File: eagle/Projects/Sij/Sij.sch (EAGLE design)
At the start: 59 parts, among them U1 ATMEGA2560AU, U2 BQ76925_PW_20, U3 LM1085_KTT_3, U4 LM7805

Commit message: joué avec le schematic et la commande digikey
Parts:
- removed C1, C2: 20pF, SparkFun-Capacitors:22PF-50V-5%(0603)
- removed JUMP_3_CELL, JUMP_4_CELL, JUMP_5_CELL, JUMP_PWR_BAT, JUMP_PWR_PROG: (no value), SparkFun-Connectors:M02PTH
- removed R1: 121, resistor:R-US_R0603
- removed Y1: (no value), SparkFun-FreqCtrl:CRYSTALHC49US
- added CRESET, C_DECOUPLING1, C_DECOUPLING2, C_DECOUPLING3, C_DECOUPLING4: 0.1uF, SparkFun-Capacitors:0.1UF-25V-5%(0603)
- added CRYSTAL: (no value), SparkFun-FreqCtrl:CRYSTALHC49US
- added C_AVCC: 0.1u, SparkFun-Capacitors:CAP0603-CAP
- added C_CRYSTAL_1, C_CRYSTAL_2: 20pF, SparkFun-Capacitors:22PF-50V-5%(0603)
- added D1, D2: 1N4004, diode:1N4004
- added D_POWER_SEL: (no value), SparkFun-DiscreteSemi:DIODESMA-ALT
- added JP1, JP2, JP3: (no value), SparkFun-Retired:JUMPER-2PTH
- added L1: 10uH, SparkFun-Passives:INDUCTOR0805
- added LED1, LED2, LED3, LED4, LED5, LED6, LED7: (no value), led:LEDCHIPLED_0805
- added Q_POWER_SEL1: MOSFET-PCHANNEL, SparkFun-DiscreteSemi:MOSFET-PCHANNEL
- added Q_POWER_SEL2: MOSFET-NCHANNELAO3404A, SparkFun-DiscreteSemi:MOSFET-NCHANNELAO3404A
- added RESET_SWITCH: SWITCH-MOMENTARY-2PTH, SparkFun-Electromechanical:SWITCH-MOMENTARY-2PTH
- added RLED1, RLED3, RLED4, RLED5, RLED6, RLED7: 56, resistor:R-US_R0603
- added RLED2: 316, resistor:R-US_R0603
- added RSCL, RSDA: 2K, resistor:R-US_R0603
- added RSS: 1K, resistor:R-US_R0603
- added R_1085: 121, resistor:R-US_R0603
- added R_PULL_DOWN_POWER_SEL, R_PULL_UP_POWER_SEL: 10K, resistor:R-US_R0603
- added R_RESET_SWITCH: 363, resistor:R-US_R0603
- added S1: (no value), SparkFun-Electromechanical:SWITCH-SPDTPTH
- added U5: TC7SU04F, SparkFun-DigitalIC:INVERTER_SOT23-5
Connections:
- new net N$14: BAT+.0, ESC1+.PAD, ESC2+.PAD, ESC3+.PAD, ESC4+.PAD, RLED2.1, S1.P, S1.S
- new net N$34: RESET_SWITCH.1, R_RESET_SWITCH.2
- new net N$36: CRYSTAL.2, C_CRYSTAL_2.2, U1.XTAL2
- new net N$37: Q_POWER_SEL1.G, Q_POWER_SEL2.D, R_PULL_UP_POWER_SEL.1
- new net N$38: LED3.A, RLED3.2
- new net N$39: LED6.A, RLED6.2
- new net N$4: CIN_7805.1, Q_POWER_SEL1.S, U4.IN
- new net N$41: LED7.A, RLED7.2
- new net N$42: RSS.1, U1.(SS/PCINT0)PB0
- new net RLED2: LED2.A, RLED2.2
- new net SCL: RSCL.2, U1.(SCL/INT0)PD0, U2.SCL
- new net SDA: RSDA.2, U1.(SDA/INT1)PD1, U2.SDA
- new net VCC1: RLED4.1, U1.(A14)PC6
- new net VCC2: RLED5.1, U1.(A13)PC5
- new net VCC3: RLED6.1
- new net VCC4: RLED7.1
- new net V_USB: D_POWER_SEL.A, ICSP.2, RLED3.1, U5.A
- net GND: now also CRESET.2, C_AVCC.2, C_CRYSTAL_1.1, C_CRYSTAL_2.1, C_DECOUPLING1.2, C_DECOUPLING2.2, C_DECOUPLING3.2, C_DECOUPLING4.2, D1.A, LED4.C, LED5.C, LED6.C, LED7.C, Q_POWER_SEL2.S, RESET_SWITCH.2, RSS.2, R_PULL_DOWN_POWER_SEL.1, U1.AGND, U5.GND; no longer C1.1, C2.1, U1.(SS/PCINT0)PB0
- net N$13: now also Q_POWER_SEL2.G, R_PULL_DOWN_POWER_SEL.2, U5.Y; no longer COUT_7805.1, JUMP_PWR_BAT.2, U4.OUT
- net N$19: now also LED4.A, RLED4.2; no longer U2.SDA
- net N$20: now also U1.PJ7
- net N$21: now also U1.PK1(ADC9/PCINT17)
- net N$22: now also U1.PK2(ADC10/PCINT18)
- net N$24: now also U1.PK3(ADC11/PCINT19)
- net N$25: now also LED5.A, RLED5.2; no longer U2.SCL
- net N$28: now also JP3.1; no longer JUMP_3_CELL.1
- net N$29: now also JP2.1, JP3.2; no longer JUMP_3_CELL.2, JUMP_4_CELL.1
- net N$3: now also CRESET.1, D1.C, D2.A, R_RESET_SWITCH.1
- net N$30: now also JP1.1, JP2.2; no longer JUMP_4_CELL.2, JUMP_5_CELL.1
- net N$32: now also R_1085.1; no longer R1.1
- net N$33: now also R_1085.2; no longer R1.2
- net N$35: now also LED1.A, RLED1.2; no longer ICSP.2, JUMP_PWR_PROG.1
- net N$5: now also C_AVCC.1, L1.2, U1.AVCC; no longer C2.2, U1.XTAL2, Y1.2
- net N$6: now also CRYSTAL.1, C_CRYSTAL_1.2; no longer C1.2, Y1.1
- net VCC: now also COUT_7805.1, C_DECOUPLING1.1, C_DECOUPLING2.1, C_DECOUPLING3.1, C_DECOUPLING4.1, D2.C, D_POWER_SEL.C, L1.1, RLED1.1, RSCL.1, RSDA.1, U4.OUT, U5.VCC; no longer JUMP_PWR_BAT.1, JUMP_PWR_PROG.2
- net V_BATT: now also JP1.2, Q_POWER_SEL1.D, R_PULL_UP_POWER_SEL.2, S1.O; no longer BAT+.0, CIN_7805.1, ESC1+.PAD, ESC2+.PAD, ESC3+.PAD, ESC4+.PAD, JUMP_5_CELL.2, U4.IN
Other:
- note added: "5V USB"
- note added: "LED indicators"
- note removed: "Need pull up resistors to VDD"
- note removed: "To ADC pin"
- note removed: "To GPIO pin"
- note removed: "to SCL of I2C on uC"
- note removed: "to SDA of I2C on uC"
- moved on the sheet: BAT+, BAT-, CBAT, CIN_1085, CIN_7805, COUT, COUT_1085, COUT_7805, J1, R2, U3, U4

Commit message: fini le schematic préliminaire+bibliothèques de partie+documentation
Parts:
- removed S1: (no value), SparkFun-Electromechanical:SWITCH-SPDTPTH
- added J_RECEIVER_GND, J_RECEIVER_SIG, J_RECEIVER_VCC: (no value), SparkFun-Connectors:M07
- added LED10, LED11, LED8, LED9: (no value), led:LEDCHIPLED_0805
- added RLED10, RLED11, RLED8, RLED9: 91, resistor:R-US_R0603
- added SG1: BUZZERPTH, SparkFun-Electromechanical:BUZZERPTH
- added U$2: M06_IMU, custom_parts:M06_IMU
- added U$3: SWITCH_3_PIN, custom_parts:SWITCH_3_PIN
- CRYSTAL: value (none) -> 16MHz
- D_POWER_SEL: value (none) -> CDBA320L
- ESC1_PWM, ESC3_PWM, ESC4_PWM: value (none) -> 640455 TE connectivity
- ICSP: device SparkFun-Connectors:M05X2SHD -> SparkFun-Connectors:M05X2NO_SILK
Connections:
- removed net VCC1: RLED4.1, U1.(A14)PC6
- removed net VCC2: RLED5.1, U1.(A13)PC5
- removed net VCC3: RLED6.1
- removed net VCC4: RLED7.1
- new net CH1: J_RECEIVER_SIG.1, U1.PJ0(RXD3/PCINT9)
- new net CH2: J_RECEIVER_SIG.2, U1.PJ1(TXD3/PCINT10)
- new net CH3: J_RECEIVER_SIG.3, U1.PJ2(XCK3/PCINT11)
- new net CH4: J_RECEIVER_SIG.4, U1.PJ3(PCINT12)
- new net CH5: J_RECEIVER_SIG.5, U1.PJ4(PCINT13)
- new net CH6: J_RECEIVER_SIG.6, U1.PJ5(PCINT14)
- new net INT_IMU: U$2.2, U1.(RXD1/INT2)PD2
- new net N$43: LED8.A, RLED8.2
- new net N$44: LED9.A, RLED9.2
- new net N$45: LED10.A, RLED10.2
- new net N$46: LED11.A, RLED11.2
- new net N$47: RLED4.1, U1.(A15)PC7
- new net N$48: RLED5.1, U1.(A14)PC6
- new net N$49: RLED6.1, U1.(A13)PC5
- new net N$50: RLED7.1, U1.(A12)PC4
- new net N$51: RLED8.1, U1.(A11)PC3
- new net N$52: RLED9.1, U1.(A10)PC2
- new net N$53: RLED10.1, U1.(A9)PC1
- new net N$54: RLED11.1, U1.(A8)PC0
- new net N$55: SG1.2, U1.PL5(OC5C)
- net GND: now also J_RECEIVER_GND.1, J_RECEIVER_GND.2, J_RECEIVER_GND.3, J_RECEIVER_GND.4, J_RECEIVER_GND.5, J_RECEIVER_GND.6, LED10.C, LED11.C, LED8.C, LED9.C, SG1.1, U$2.1, U$2.5
- net N$14: now also U$3.P, U$3.S; no longer S1.P, S1.S
- net SCL: now also U$2.3
- net SDA: now also U$2.4
- net VCC: now also J_RECEIVER_VCC.1, J_RECEIVER_VCC.2, J_RECEIVER_VCC.3, J_RECEIVER_VCC.4, J_RECEIVER_VCC.5, J_RECEIVER_VCC.6, U$2.6
- net V_BATT: now also U$3.O; no longer S1.O
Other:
- note added: "Crystal"
- note added: "IMU"
- note added: "Programmer"
- note added: "RF"
- note added: "Reset"
- moved on the sheet: LED4, LED5, LED6, LED7, RLED4, RLED5, RLED6, RLED7

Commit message: listes matériel
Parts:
- CSENSE: device rcl:C-USC0805 -> SparkFun-Passives:CAP0603-CAP
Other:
- moved on the sheet: CSENSE
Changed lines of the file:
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@@
 <part name="CIN6" library="SparkFun-Capacitors" deviceset="1.0UF-16V-10%(0603)" device="" value="1.0uF"/>
 <part name="GND4" library="SparkFun-Aesthetics" deviceset="GND" device=""/>
-<part name="CSENSE" library="rcl" deviceset="C-US" device="C0805" value="0.1u"/>
+<part name="CSENSE" library="SparkFun-Passives" deviceset="CAP" device="0603-CAP" value="0.1u"/>
 <part name="RSENSEN" library="resistor" deviceset="R-US_" device="R0603" value="1K"/>
 <part name="RSENSEP" library="resistor" deviceset="R-US_" device="R0603" value="1K"/>
@@
 <wire x1="-325.12" y1="-5.08" x2="-325.12" y2="0" width="0.1524" layer="91"/>
 <pinref part="CSENSE" gate="G$1" pin="1"/>
-<wire x1="-325.12" y1="0" x2="-322.58" y2="0" width="0.1524" layer="91"/>
 <wire x1="-325.12" y1="0" x2="-325.12" y2="7.62" width="0.1524" layer="91"/>
 <junction x="-325.12" y="0"/>
@@
 <pinref part="RSENSEP" gate="G$1" pin="2"/>
 <pinref part="CSENSE" gate="G$1" pin="2"/>
-<wire x1="-314.96" y1="-5.08" x2="-314.96" y2="0" width="0.1524" layer="91"/>
-<wire x1="-314.96" y1="0" x2="-284.48" y2="0" width="0.1524" layer="91"/>
+<wire x1="-314.96" y1="-5.08" x2="-317.5" y2="0" width="0.1524" layer="91"/>
+<wire x1="-317.5" y1="0" x2="-284.48" y2="0" width="0.1524" layer="91"/>
 <wire x1="-284.48" y1="0" x2="-284.48" y2="20.32" width="0.1524" layer="91"/>
-<junction x="-314.96" y="0"/>
+<junction x="-317.5" y="0"/>
 <pinref part="U2" gate="A" pin="SENSEP"/>
 <wire x1="-284.48" y1="20.32" x2="-287.02" y2="20.32" width="0.1524" layer="91"/>

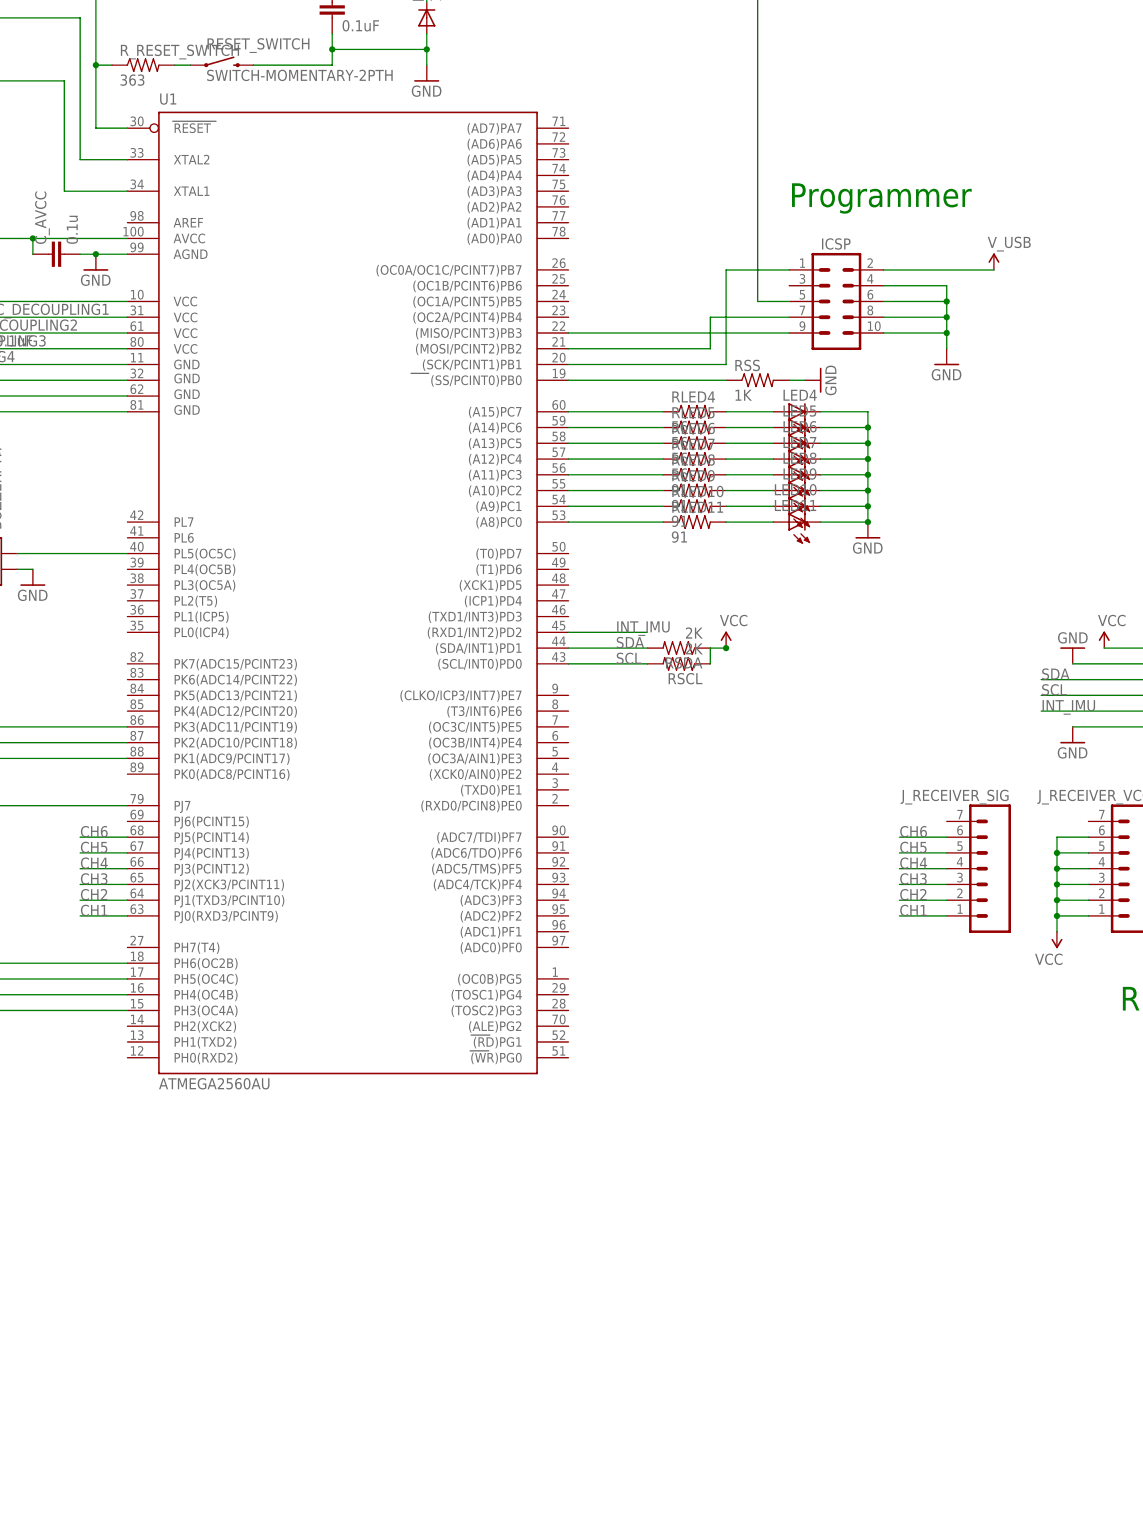
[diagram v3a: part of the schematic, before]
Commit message: quelques ports ajoutés
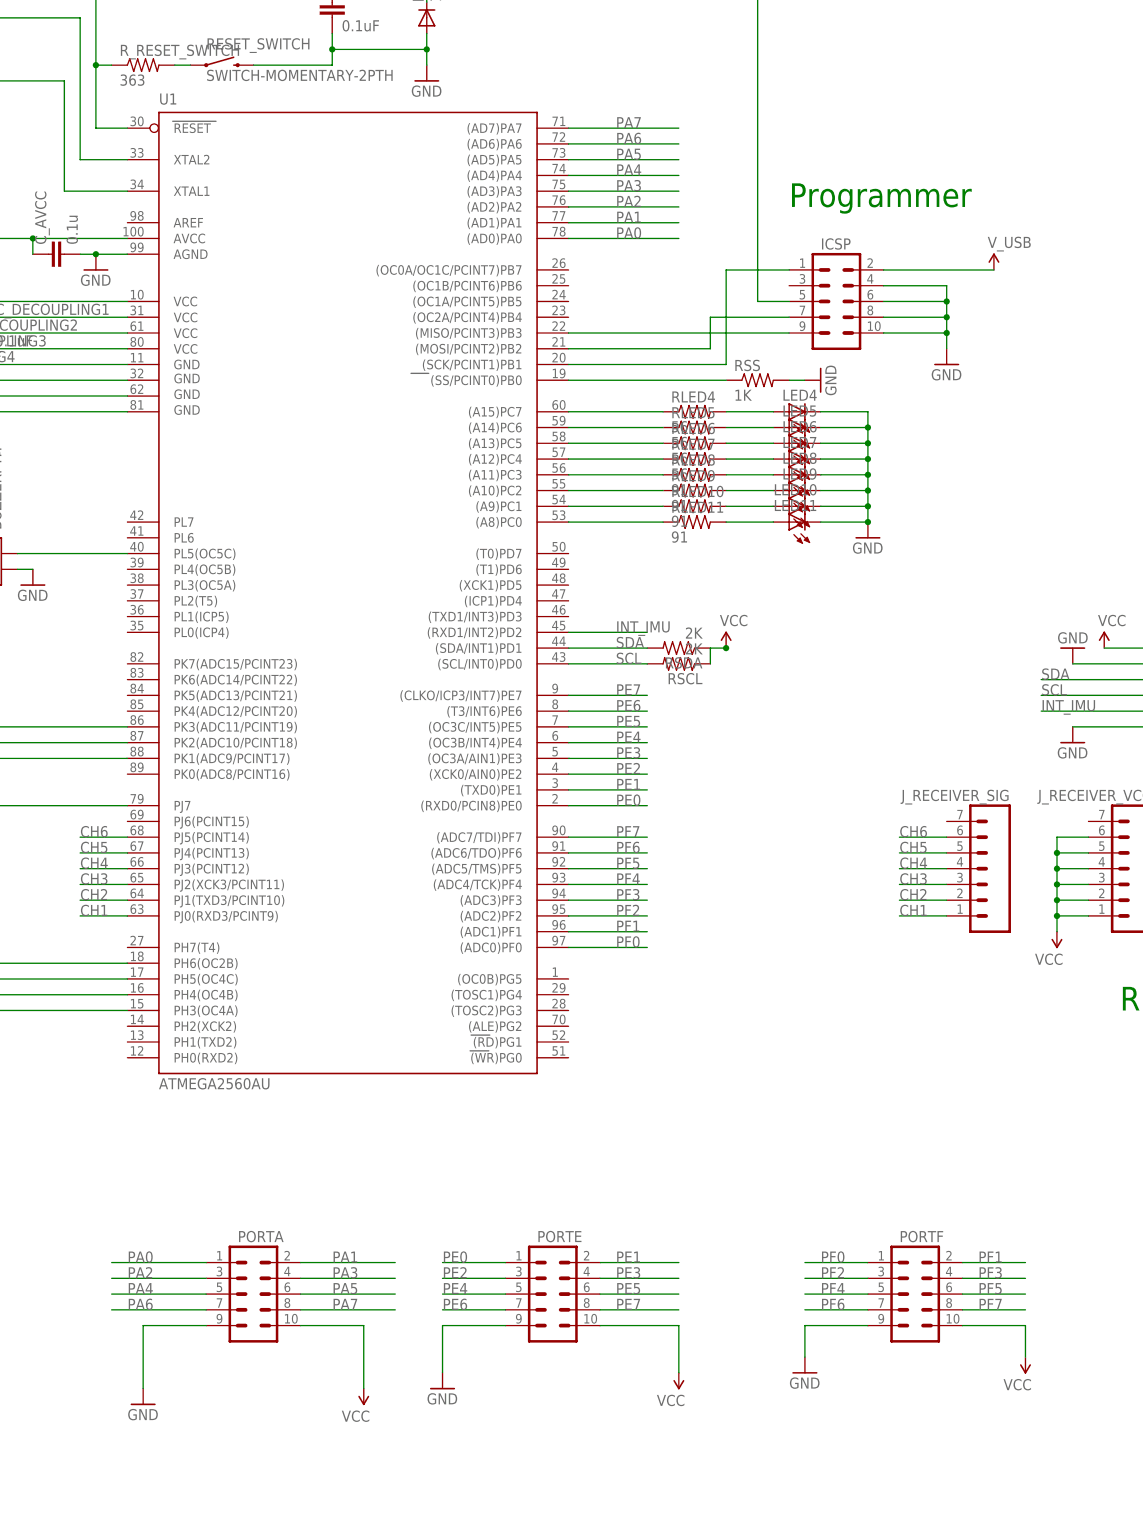
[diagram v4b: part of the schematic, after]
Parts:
- added PORTA, PORTE, PORTF: (no value), SparkFun-Connectors:M05X2PTH
- ICSP: device SparkFun-Connectors:M05X2NO_SILK -> SparkFun-Connectors:M05X2PTH
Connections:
- new net PA0: PORTA.1, U1.(AD0)PA0
- new net PA1: PORTA.2, U1.(AD1)PA1
- new net PA2: PORTA.3, U1.(AD2)PA2
- new net PA3: PORTA.4, U1.(AD3)PA3
- new net PA4: PORTA.5, U1.(AD4)PA4
- new net PA5: PORTA.6, U1.(AD5)PA5
- new net PA6: PORTA.7, U1.(AD6)PA6
- new net PA7: PORTA.8, U1.(AD7)PA7
- new net PE0: PORTE.1, U1.(RXD0/PCIN8)PE0
- new net PE1: PORTE.2, U1.(TXD0)PE1
- new net PE2: PORTE.3, U1.(XCK0/AIN0)PE2
- new net PE3: PORTE.4, U1.(OC3A/AIN1)PE3
- new net PE4: PORTE.5, U1.(OC3B/INT4)PE4
- new net PE5: PORTE.6, U1.(OC3C/INT5)PE5
- new net PE6: PORTE.7, U1.(T3/INT6)PE6
- new net PE7: PORTE.8, U1.(CLKO/ICP3/INT7)PE7
- new net PF0: PORTF.1, U1.(ADC0)PF0
- new net PF1: PORTF.2, U1.(ADC1)PF1
- new net PF2: PORTF.3, U1.(ADC2)PF2
- new net PF3: PORTF.4, U1.(ADC3)PF3
- new net PF4: PORTF.5, U1.(ADC4/TCK)PF4
- new net PF5: PORTF.6, U1.(ADC5/TMS)PF5
- new net PF6: PORTF.7, U1.(ADC6/TDO)PF6
- new net PF7: PORTF.8, U1.(ADC7/TDI)PF7
- net GND: now also PORTA.9, PORTE.9, PORTF.9
- net VCC: now also PORTA.10, PORTE.10, PORTF.10

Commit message: quelques ports
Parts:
- added SV1, SV2, SV3: (no value), con-lstb:MA10-1W
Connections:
- new net N$101: U1.PH2(XCK2)
- new net N$102: U1.PH1(TXD2)
- new net N$103: U1.PH0(RXD2)
- new net N$56: SV1.1
- new net N$57: SV1.2
- new net N$58: SV1.3
- new net N$59: SV1.4
- new net N$60: SV1.5
- new net N$66: SV2.10
- new net N$67: SV2.9
- new net N$68: SV2.8
- new net N$69: SV2.7
- new net N$70: SV2.6
- new net N$71: SV2.5
- new net N$72: SV2.4
- new net N$73: SV2.3
- new net N$74: SV2.2
- new net N$75: SV2.1
- new net N$76: SV3.10
- new net N$77: SV3.9
- new net N$78: SV3.8
- new net N$79: SV3.7
- new net N$80: SV3.6
- new net N$81: SV3.5
- new net N$82: SV3.4
- new net N$83: SV3.3
- new net N$84: SV3.2
- new net N$85: SV3.1
- new net PB4: SV1.7, U1.(OC2A/PCINT4)PB4
- new net PB5: SV1.8, U1.(OC1A/PCINT5)PB5
- new net PB6: SV1.9, U1.(OC1B/PCINT6)PB6
- new net PB7: SV1.10, U1.(OC0A/OC1C/PCINT7)PB7
- new net PD3: U1.(TXD1/INT3)PD3
- new net PD4: U1.(ICP1)PD4
- new net PD5: U1.(XCK1)PD5
- new net PD6: U1.(T1)PD6
- new net PD7: U1.(T0)PD7
- new net PG0: U1.(WR)PG0
- new net PG1: U1.(RD)PG1
- new net PG2: U1.(ALE)PG2
- new net PG3: U1.(TOSC2)PG3
- new net PG4: U1.(TOSC1)PG4
- new net PG5: SV1.6, U1.(OC0B)PG5
